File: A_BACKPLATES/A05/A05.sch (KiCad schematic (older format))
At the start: 72 parts, among them J0 Conn_01x01_Male, J1 Conn_01x01_Male, J2 Conn_01x01_Male, J3 Conn_01x01_Male

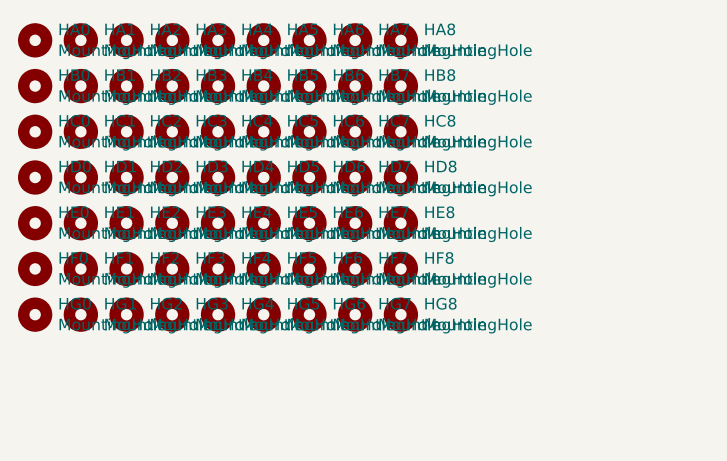
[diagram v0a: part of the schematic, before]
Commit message: fixed misplaced mounting hole
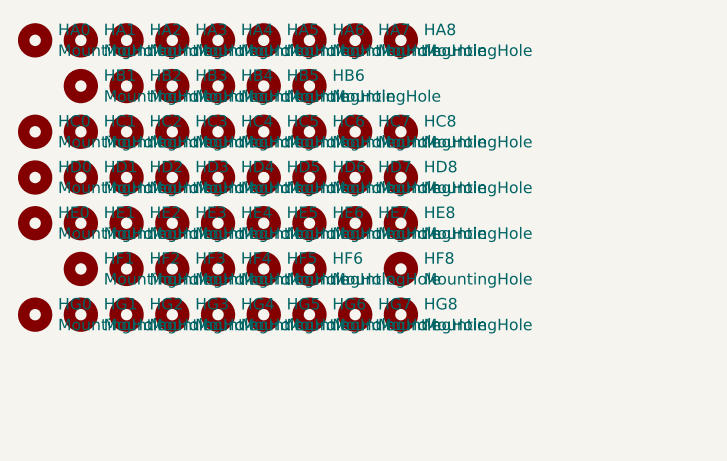
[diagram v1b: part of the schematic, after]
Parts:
- removed HB0, HB7, HB8, HF0, HF7: MountingHole, MountingHole:MountingHole_3mm, symbol Mechanical:MountingHole
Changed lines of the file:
@@
-$EndComp
-$Comp
-L Mechanical:MountingHole HB0
-U 1 1 5F3277F5
-P 800 900
-F 0 "HB0" H 900 946 50  0000 L CNN
-F 1 "MountingHole" H 900 855 50  0000 L CNN
-F 2 "MountingHole:MountingHole_3mm" H 800 900 50  0001 C CNN
-F 3 "~" H 800 900 50  0001 C CNN
-	1    800  900
-	1    0    0    -1
 $EndComp
 $Comp
@@
 $EndComp
 $Comp
-L Mechanical:MountingHole HF0
-U 1 1 5F328807
-P 800 1700
-F 0 "HF0" H 900 1746 50  0000 L CNN
-F 1 "MountingHole" H 900 1655 50  0000 L CNN
-F 2 "MountingHole:MountingHole_3mm" H 800 1700 50  0001 C CNN
-F 3 "~" H 800 1700 50  0001 C CNN
-	1    800  1700
-	1    0    0    -1
-$EndComp
-$Comp
 L Mechanical:MountingHole HG0
 U 1 1 5F32A604
@@
 $EndComp
 $Comp
-L Mechanical:MountingHole HB7
-U 1 1 5F34255F
-P 2200 900
-F 0 "HB7" H 2300 946 50  0000 L CNN
-F 1 "MountingHole" H 2300 855 50  0000 L CNN
-F 2 "MountingHole:MountingHole_3mm" H 2200 900 50  0001 C CNN
-F 3 "~" H 2200 900 50  0001 C CNN
-	1    2200 900
-	1    0    0    -1
-$EndComp
-$Comp
 L Mechanical:MountingHole HC7
 U 1 1 5F342D1B
@@
 $EndComp
 $Comp
-L Mechanical:MountingHole HF7
-U 1 1 5F344477
-P 2200 1700
-F 0 "HF7" H 2300 1746 50  0000 L CNN
-F 1 "MountingHole" H 2300 1655 50  0000 L CNN
-F 2 "MountingHole:MountingHole_3mm" H 2200 1700 50  0001 C CNN
-F 3 "~" H 2200 1700 50  0001 C CNN
-	1    2200 1700
-	1    0    0    -1
-$EndComp
-$Comp
 L Mechanical:MountingHole HG7
 U 1 1 5F344D3A
@@
 	1    0    0    -1
 $EndComp
-$Comp
-L Mechanical:MountingHole HB8
-U 1 1 5F345D8B
-P 2400 900
-F 0 "HB8" H 2500 946 50  0000 L CNN
-F 1 "MountingHole" H 2500 855 50  0000 L CNN
-F 2 "MountingHole:MountingHole_3mm" H 2400 900 50  0001 C CNN
-F 3 "~" H 2400 900 50  0001 C CNN
-	1    2400 900
-	1    0    0    -1
-$EndComp
